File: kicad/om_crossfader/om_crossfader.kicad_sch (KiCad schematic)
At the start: 16 parts, among them U1 Opamp_Quad, U2 Opamp_Quad

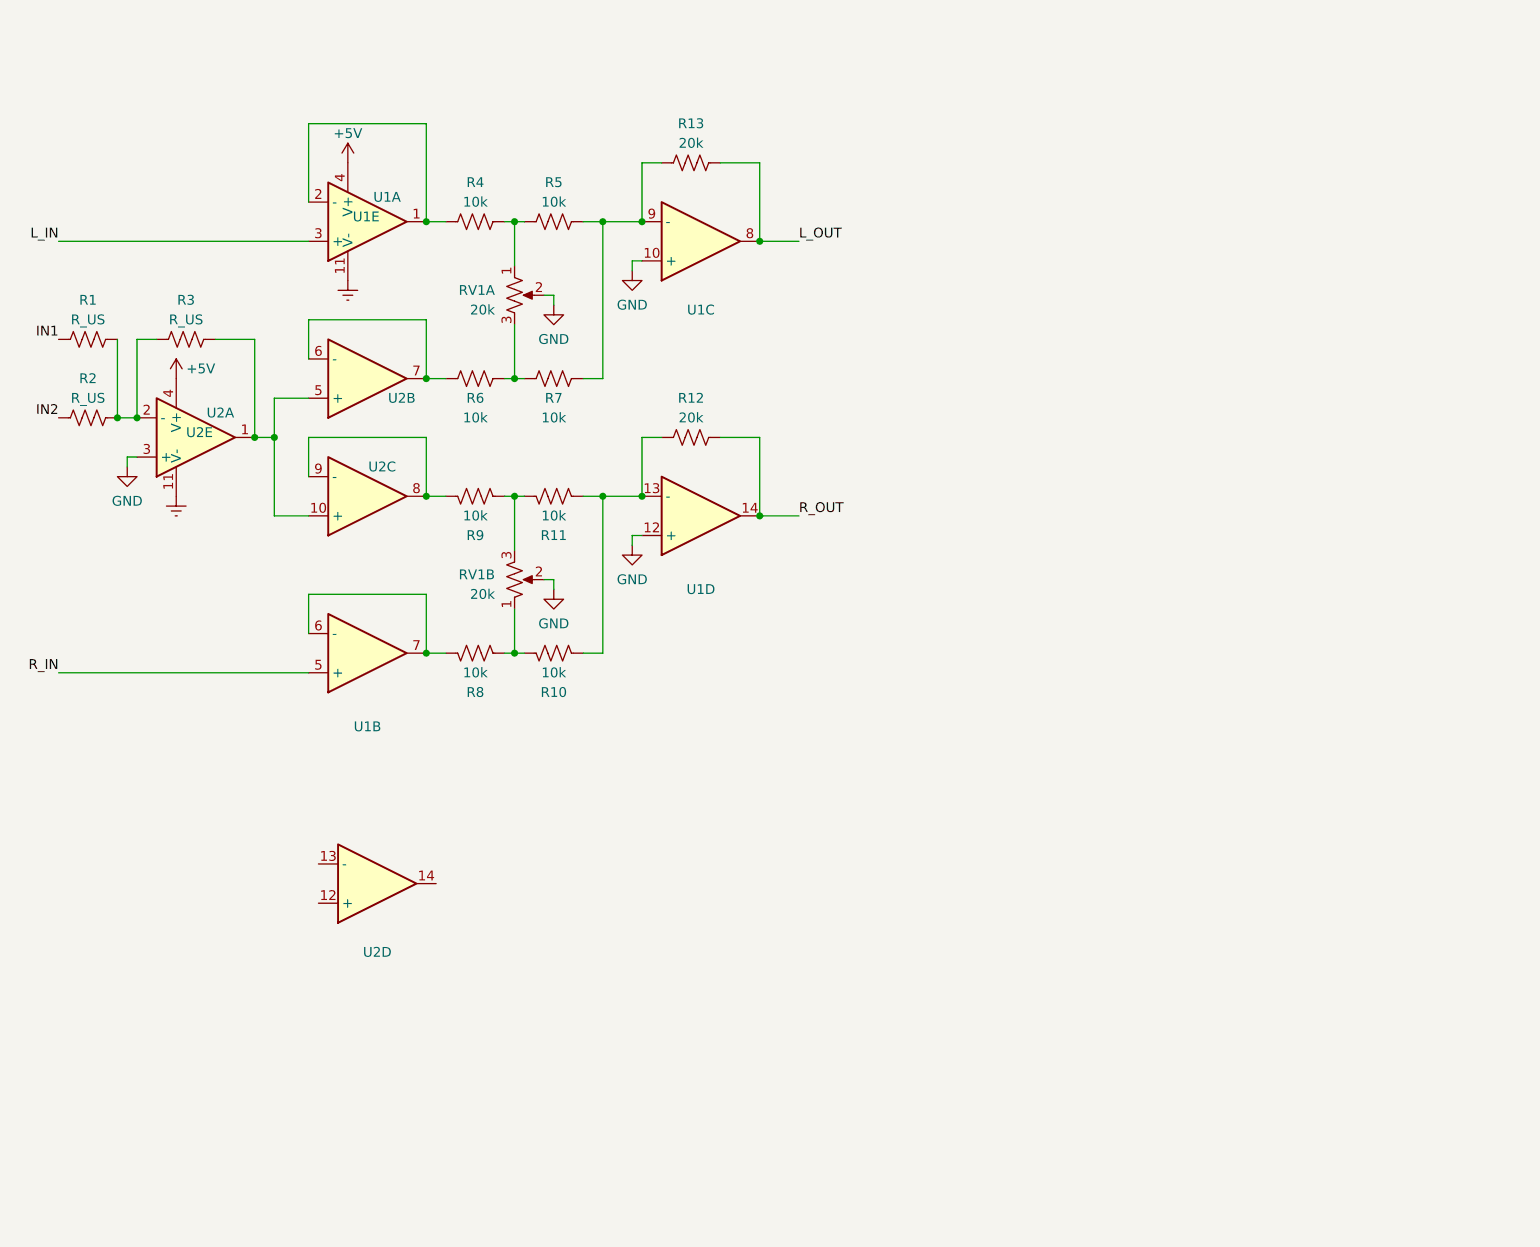
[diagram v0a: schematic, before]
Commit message: crossfader improvements
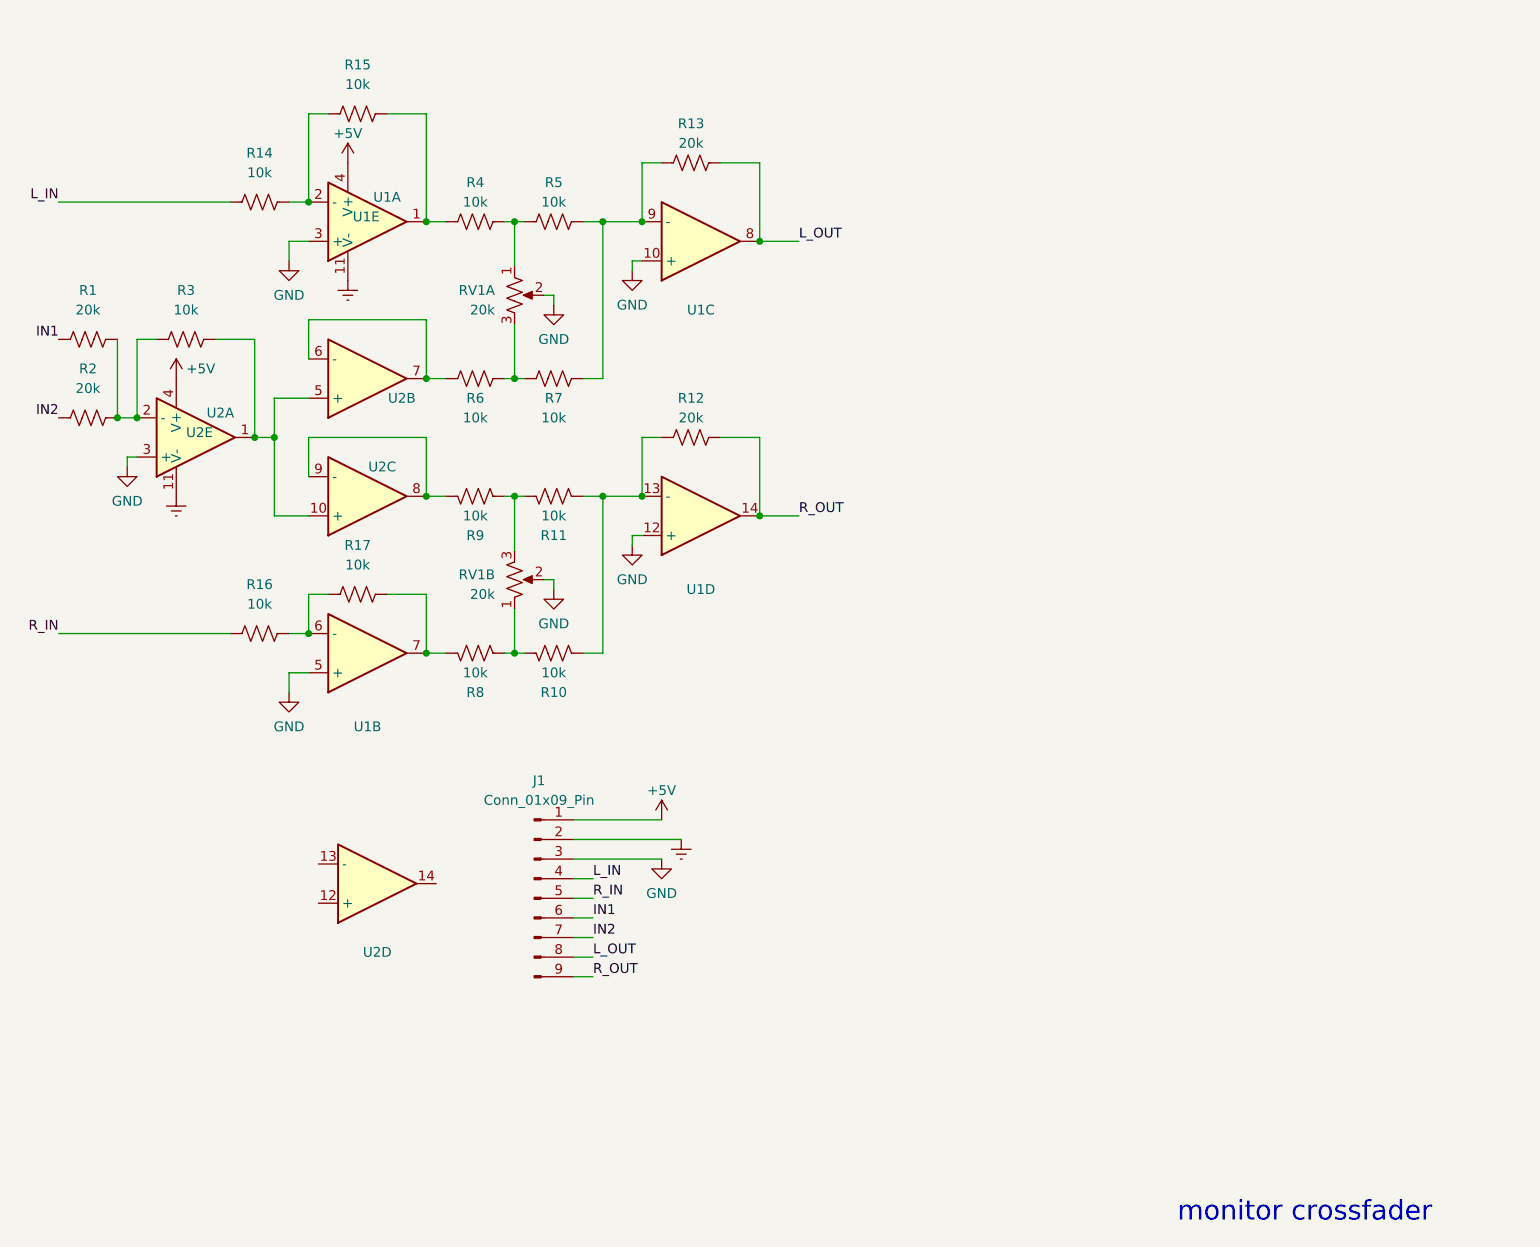
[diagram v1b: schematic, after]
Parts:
- added J1: Conn_01x09_Pin, symbol Connector:Conn_01x09_Pin
- added R14, R15, R16, R17: 10k, symbol Device:R_US
- R1, R2: value R_US -> 20k
- R3: value R_US -> 10k
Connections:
- net +5V: now also J1.1 (Pin_1)
- net Earth: now also J1.2 (Pin_2)
- net GND: now also U1.3 (+), U1.5 (+), J1.3 (Pin_3)
- net IN1: now also J1.6 (Pin_6)
- net IN2: now also J1.7 (Pin_7)
- net L_IN: now also J1.4 (Pin_4), R14.1; no longer U1.3 (+)
- net L_OUT: now also J1.8 (Pin_8)
- net R_IN: now also J1.5 (Pin_5), R16.1; no longer U1.5 (+)
- net R_OUT: now also J1.9 (Pin_9)
- net at R4.1, U1.1: now also R15.2; no longer U1.2 (-)
- net at R8.1, U1.7: now also R17.2; no longer U1.6 (-)
- new net: R16.2, R17.1, U1.6 (-)
- new net: R14.2, R15.1, U1.2 (-)
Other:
- note added: "monitor crossfader"

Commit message: 15v rails and 5532 amp
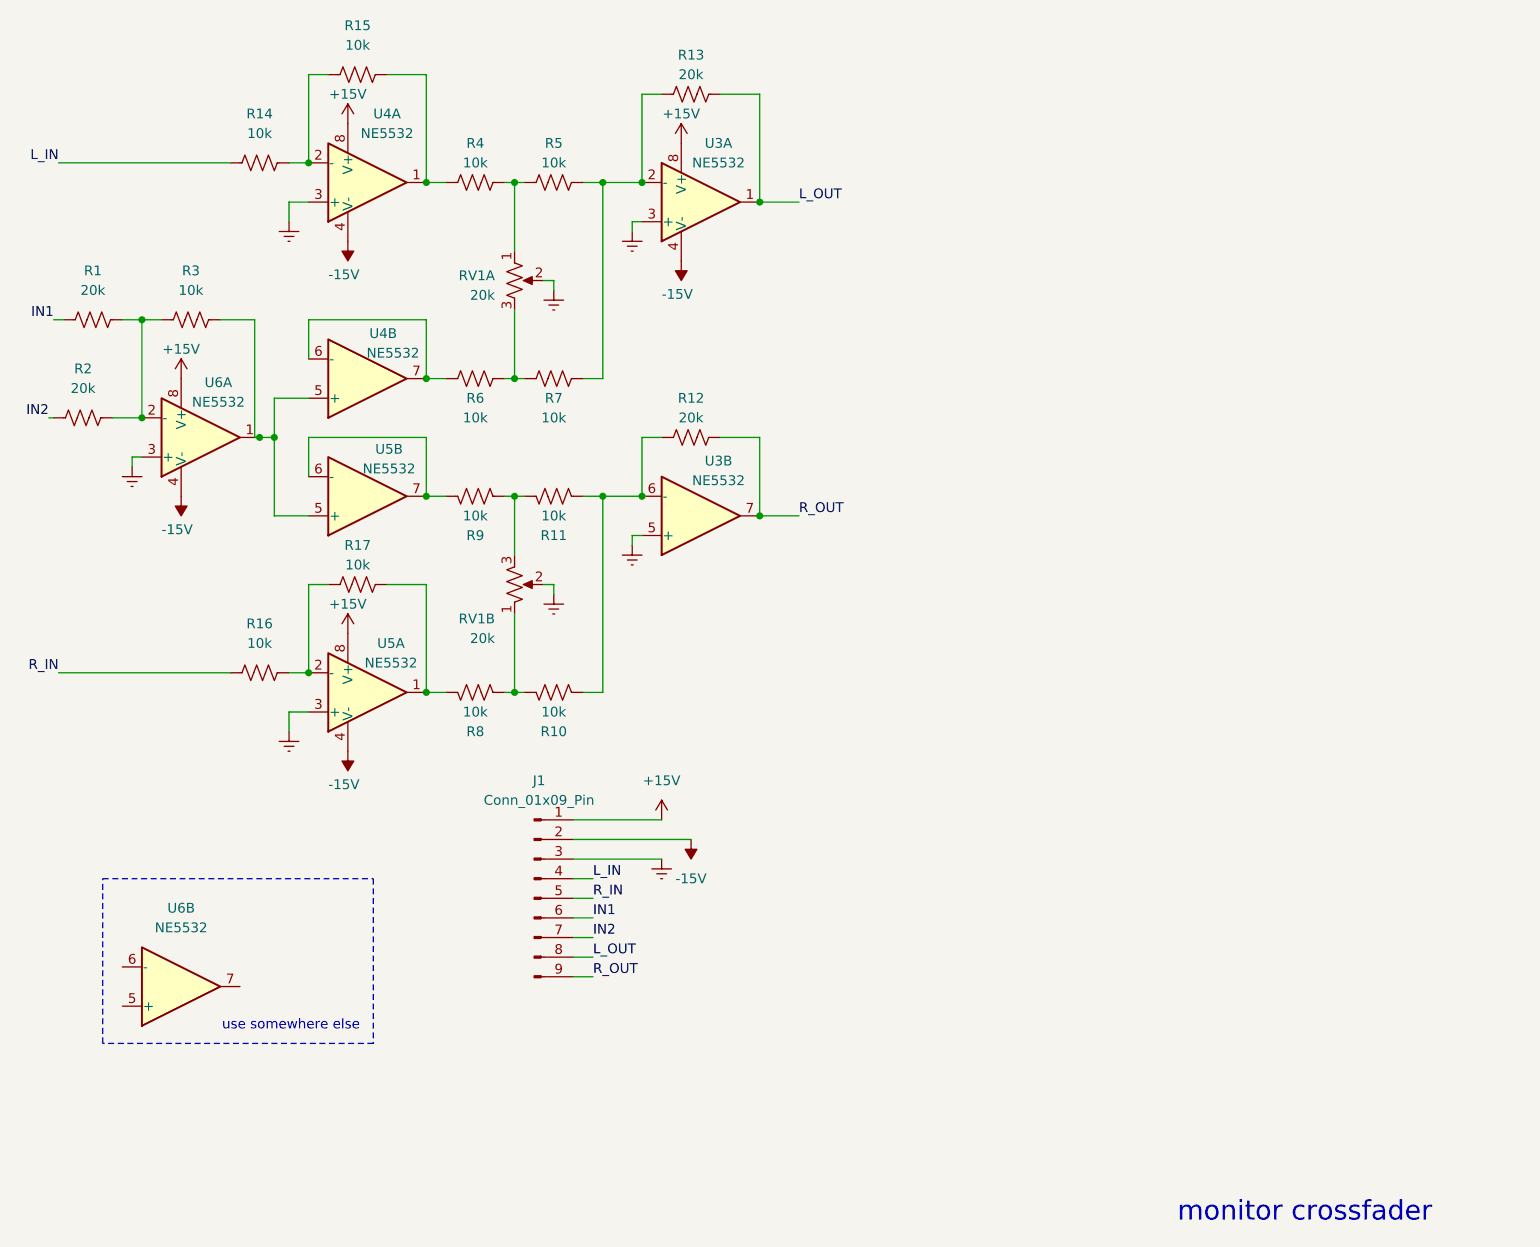
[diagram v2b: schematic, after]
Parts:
- removed U1, U2: Opamp_Quad, symbol Device:Opamp_Quad
- added U3, U4, U5, U6: NE5532, symbol Amplifier_Operational:NE5532
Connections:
- net GND is gone; now on net Earth: J1.3 (Pin_3), RV1.2, RV1.2
- net Earth: now also U3.3 (+), U3.5 (+), U4.3 (+), U5.3 (+), U6.3 (+); no longer J1.2 (Pin_2)
- net L_OUT: now also U3.1
- net R_OUT: now also U3.7
- net at R13.1, R5.2, R7.2: now also U3.2 (-)
- net at R1.2, R2.2, R3.1: now also U6.2 (-)
- net at R3.2: now also U4.5 (+), U5.5 (+), U6.1
- net at R15.2, R4.1: now also U4.1
- net at R9.1: now also U5.6 (-), U5.7
- net at R16.2, R17.1: now also U5.2 (-)
- net at R17.2, R8.1: now also U5.1
- net at R10.2, R11.2, R12.1: now also U3.6 (-)
- net at R14.2, R15.1: now also U4.2 (-)
- net at R6.1: now also U4.6 (-), U4.7
- net +5V renamed +15V
- net +15V: now also U3.8 (V+), U4.8 (V+), U5.8 (V+), U6.8 (V+)
- new net -15V: J1.2 (Pin_2), U3.4 (V-), U4.4 (V-), U5.4 (V-), U6.4 (V-)
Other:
- note added: "use somewhere else"
- moved on the sheet: R1, R10, R13, R14, R15, R16, R17, R2, R3, R4, R5, R8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
